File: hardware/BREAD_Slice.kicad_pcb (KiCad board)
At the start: 2 copper layers, 70 x 100 mm, 15 parts, among them J1 Conn_01x10_Female

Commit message: completed schematic and board
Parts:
- added C10: 10u X7R, Capacitor_SMD:C_1206_3216Metric_Pad1.33x1.80mm_HandSolder, F.Cu at (90.9, 107.4)
- added C11: 0.1u X7R, Capacitor_SMD:C_1206_3216Metric_Pad1.33x1.80mm_HandSolder, F.Cu at (94.8, 109.4)
- added C12: 1u X7R, Capacitor_SMD:C_1206_3216Metric_Pad1.33x1.80mm_HandSolder, F.Cu at (97.5, 109.4)
- added C13: 10u X5R, Capacitor_SMD:C_1206_3216Metric_Pad1.33x1.80mm_HandSolder, F.Cu at (86.2, 106.4)
- added C14: 10u, Capacitor_SMD:C_0805_2012Metric_Pad1.18x1.45mm_HandSolder, F.Cu at (67.8, 118.6)
- added C15: 10n, Capacitor_SMD:C_0805_2012Metric_Pad1.18x1.45mm_HandSolder, F.Cu at (67.8, 122.8)
- added C16: 10n, Capacitor_SMD:C_0805_2012Metric_Pad1.18x1.45mm_HandSolder, F.Cu at (82.3, 122.9)
- added C17: 10u, Capacitor_SMD:C_0805_2012Metric_Pad1.18x1.45mm_HandSolder, F.Cu at (79.8, 127.3)
- added C18: 0.01u, Capacitor_SMD:C_0603_1608Metric_Pad1.08x0.95mm_HandSolder, F.Cu at (139.0, 132.9)
- added C19: 0.1u, Capacitor_SMD:C_0603_1608Metric_Pad1.08x0.95mm_HandSolder, F.Cu at (105.1, 104.6)
- added C20: 0.1u, Capacitor_SMD:C_0603_1608Metric_Pad1.08x0.95mm_HandSolder, F.Cu at (105.1, 101.3)
- added C21: 0.01u, Capacitor_SMD:C_0603_1608Metric_Pad1.08x0.95mm_HandSolder, F.Cu at (139.1, 108.9)
- added C22: 0.1u, Capacitor_SMD:C_0603_1608Metric_Pad1.08x0.95mm_HandSolder, F.Cu at (105.0, 98.1)
- added C23: 0.1u, Capacitor_SMD:C_0603_1608Metric_Pad1.08x0.95mm_HandSolder, F.Cu at (105.1, 96.2)
- added C24: 0.01u, Capacitor_SMD:C_0603_1608Metric_Pad1.08x0.95mm_HandSolder, F.Cu at (139.2, 84.5)
- added C25: 0.1u, Capacitor_SMD:C_0603_1608Metric_Pad1.08x0.95mm_HandSolder, F.Cu at (104.6, 91.3)
- added C26: 0.1u, Capacitor_SMD:C_0603_1608Metric_Pad1.08x0.95mm_HandSolder, F.Cu at (102.7, 91.3)
- added C27: 0.01u, Capacitor_SMD:C_0603_1608Metric_Pad1.08x0.95mm_HandSolder, F.Cu at (117.1, 54.6)
- added C28: 0.1u, Capacitor_SMD:C_0603_1608Metric_Pad1.08x0.95mm_HandSolder, F.Cu at (99.5, 91.3)
- added C29: 0.1u, Capacitor_SMD:C_0603_1608Metric_Pad1.08x0.95mm_HandSolder, F.Cu at (94.8, 91.3)
- added C30: 0.01u, Capacitor_SMD:C_0603_1608Metric_Pad1.08x0.95mm_HandSolder, F.Cu at (89.0, 54.4)
- added C31: 0.1u, Capacitor_SMD:C_0603_1608Metric_Pad1.08x0.95mm_HandSolder, F.Cu at (93.0, 91.3)
- added C32: 0.1u, Capacitor_SMD:C_0603_1608Metric_Pad1.08x0.95mm_HandSolder, F.Cu at (89.9, 91.3)
- added C5: 0.01u, Capacitor_SMD:C_0603_1608Metric_Pad1.08x0.95mm_HandSolder, F.Cu at (139.1, 157.3)
- added C6: 0.1u, Capacitor_SMD:C_0603_1608Metric_Pad1.08x0.95mm_HandSolder, F.Cu at (102.2, 108.8)
- added C7: 0.1u, Capacitor_SMD:C_0603_1608Metric_Pad1.08x0.95mm_HandSolder, F.Cu at (104.1, 108.8)
- added C8: 0.1u X7R, Capacitor_SMD:C_0603_1608Metric_Pad1.08x0.95mm_HandSolder, F.Cu at (87.0, 104.3)
- added C9: 10u X7R, Capacitor_SMD:C_1206_3216Metric_Pad1.33x1.80mm_HandSolder, F.Cu at (86.2, 102.2)
- added D10: DF2S6.8MFS_L3M, Diode_SMD:D_SOD-923, B.Cu at (142.1, 114.4)
- added D11: DF2S6.8MFS_L3M, Diode_SMD:D_SOD-923, B.Cu at (135.4, 114.4)
- added D12: DF2S6.8MFS_L3M, Diode_SMD:D_SOD-923, B.Cu at (142.2, 101.9)
- added D13: DF2S6.8MFS_L3M, Diode_SMD:D_SOD-923, B.Cu at (135.2, 101.9)
- added D14: DF2S6.8MFS_L3M, Diode_SMD:D_SOD-923, B.Cu at (142.1, 90.0)
- added D15: DF2S6.8MFS_L3M, Diode_SMD:D_SOD-923, B.Cu at (135.3, 90.0)
- added D16: DF2S6.8MFS_L3M, Diode_SMD:D_SOD-923, B.Cu at (142.1, 77.6)
- added D17: DF2S6.8MFS_L3M, Diode_SMD:D_SOD-923, B.Cu at (135.2, 77.6)
- added D18: DF2S6.8MFS_L3M, Diode_SMD:D_SOD-923, B.Cu at (122.6, 51.7)
- added D19: DF2S6.8MFS_L3M, Diode_SMD:D_SOD-923, B.Cu at (122.6, 58.4)
- added D2: DF2S6.8MFS_L3M, Diode_SMD:D_SOD-923, B.Cu at (142.0, 162.8)
- added D20: DF2S6.8MFS_L3M, Diode_SMD:D_SOD-923, B.Cu at (110.2, 51.6)
- added D21: DF2S6.8MFS_L3M, Diode_SMD:D_SOD-923, B.Cu at (110.2, 58.6)
- added D22: DF2S6.8MFS_L3M, Diode_SMD:D_SOD-923, B.Cu at (94.5, 51.6)
- added D23: DF2S6.8MFS_L3M, Diode_SMD:D_SOD-923, B.Cu at (94.5, 58.3)
- added D24: DF2S6.8MFS_L3M, Diode_SMD:D_SOD-923, B.Cu at (82.0, 51.5)
- added D25: DF2S6.8MFS_L3M, Diode_SMD:D_SOD-923, B.Cu at (82.0, 58.5)
- added D3: DF2S6.8MFS_L3M, Diode_SMD:D_SOD-923, B.Cu at (135.3, 162.7)
- added D4: DF2S6.8MFS_L3M, Diode_SMD:D_SOD-923, B.Cu at (142.1, 150.3)
- added D5: DF2S6.8MFS_L3M, Diode_SMD:D_SOD-923, B.Cu at (135.1, 150.3)
- added D6: DF2S6.8MFS_L3M, Diode_SMD:D_SOD-923, B.Cu at (142.0, 138.4)
- added D7: DF2S6.8MFS_L3M, Diode_SMD:D_SOD-923, B.Cu at (135.3, 138.4)
- added D8: DF2S6.8MFS_L3M, Diode_SMD:D_SOD-923, B.Cu at (142.1, 126.0)
- added D9: DF2S6.8MFS_L3M, Diode_SMD:D_SOD-923, B.Cu at (135.1, 126.0)
- added J10: PCC-SMP-V-K, kml-custom:OMEGA_PCC-SMP-V-K, F.Cu at (132.3, 126.0)
- added J11: PCC-SMP-V-K, kml-custom:OMEGA_PCC-SMP-V-K, F.Cu at (132.4, 101.9)
- added J12: PCC-SMP-V-K, kml-custom:OMEGA_PCC-SMP-V-K, F.Cu at (132.4, 77.6)
- added J13: PCC-SMP-V-K, kml-custom:OMEGA_PCC-SMP-V-K, F.Cu at (110.1, 61.4)
- added J14: PCC-SMP-V-K, kml-custom:OMEGA_PCC-SMP-V-K, F.Cu at (82.0, 61.3)
- added J2: Conn_01x03_Pin, Connector_PinHeader_2.54mm:PinHeader_1x03_P2.54mm_Vertical, F.Cu at (81.4, 89.7)
- added J3: PCC-SMP-V-K, kml-custom:OMEGA_PCC-SMP-V-K, F.Cu at (132.3, 162.7)
- added J4: PCC-SMP-V-K, kml-custom:OMEGA_PCC-SMP-V-K, F.Cu at (132.3, 138.4)
- added J5: PCC-SMP-V-K, kml-custom:OMEGA_PCC-SMP-V-K, F.Cu at (132.4, 114.4)
- added J6: PCC-SMP-V-K, kml-custom:OMEGA_PCC-SMP-V-K, F.Cu at (132.4, 90.0)
- added J7: PCC-SMP-V-K, kml-custom:OMEGA_PCC-SMP-V-K, F.Cu at (122.6, 61.4)
- added J8: PCC-SMP-V-K, kml-custom:OMEGA_PCC-SMP-V-K, F.Cu at (94.5, 61.3)
- added J9: PCC-SMP-V-K, kml-custom:OMEGA_PCC-SMP-V-K, F.Cu at (132.3, 150.3)
- added NT1: NetTie_2, NetTie:NetTie-2_SMD_Pad2.0mm, B.Cu at (63.7, 156.4)
- added NT2: NetTie_2, NetTie:NetTie-2_SMD_Pad2.0mm, F.Cu at (73.4, 125.4)
- added Q1: 2N3904, Package_TO_SOT_THT:TO-92_Inline, F.Cu at (135.4, 156.9)
- added Q2: 2N3904, Package_TO_SOT_THT:TO-92_Inline, F.Cu at (135.4, 132.5)
- added Q3: 2N3904, Package_TO_SOT_THT:TO-92_Inline, F.Cu at (135.5, 108.5)
- added Q4: 2N3904, Package_TO_SOT_THT:TO-92_Inline, F.Cu at (135.5, 84.2)
- added Q5: 2N3904, Package_TO_SOT_THT:TO-92_Inline, F.Cu at (116.7, 58.3)
- added Q6: 2N3904, Package_TO_SOT_THT:TO-92_Inline, F.Cu at (88.6, 58.2)
- added R1: 1k, Resistor_SMD:R_0603_1608Metric_Pad0.98x0.95mm_HandSolder, F.Cu at (85.0, 93.1)
- added R10: 1k, Resistor_SMD:R_0603_1608Metric_Pad0.98x0.95mm_HandSolder, F.Cu at (117.5, 136.7)
- added R11: 1k, Resistor_SMD:R_0603_1608Metric_Pad0.98x0.95mm_HandSolder, F.Cu at (105.1, 102.8)
- added R12: 1k, Resistor_SMD:R_0603_1608Metric_Pad0.98x0.95mm_HandSolder, F.Cu at (127.0, 126.0)
- added R13: 1k, Resistor_SMD:R_0603_1608Metric_Pad0.98x0.95mm_HandSolder, F.Cu at (105.0, 99.7)
- added R14: 1k, Resistor_SMD:R_0603_1608Metric_Pad0.98x0.95mm_HandSolder, F.Cu at (117.4, 112.6)
- added R15: 1k, Resistor_SMD:R_0603_1608Metric_Pad0.98x0.95mm_HandSolder, F.Cu at (105.1, 94.7)
- added R16: 1k, Resistor_SMD:R_0603_1608Metric_Pad0.98x0.95mm_HandSolder, F.Cu at (127.0, 101.9)
- added R17: 1k, Resistor_SMD:R_0603_1608Metric_Pad0.98x0.95mm_HandSolder, F.Cu at (106.1, 91.3)
- added R18: 1k, Resistor_SMD:R_0603_1608Metric_Pad0.98x0.95mm_HandSolder, F.Cu at (117.6, 88.3)
- added R19: 1k, Resistor_SMD:R_0603_1608Metric_Pad0.98x0.95mm_HandSolder, F.Cu at (101.1, 91.3)
- added R2: 1k, Resistor_SMD:R_0603_1608Metric_Pad0.98x0.95mm_HandSolder, F.Cu at (85.0, 95.8)
- added R20: 1k, Resistor_SMD:R_0603_1608Metric_Pad0.98x0.95mm_HandSolder, F.Cu at (127.0, 77.6)
- added R21: 1k, Resistor_SMD:R_0603_1608Metric_Pad0.98x0.95mm_HandSolder, F.Cu at (98.0, 91.3)
- added R22: 1k, Resistor_SMD:R_0603_1608Metric_Pad0.98x0.95mm_HandSolder, F.Cu at (120.9, 76.3)
- added R23: 1k, Resistor_SMD:R_0603_1608Metric_Pad0.98x0.95mm_HandSolder, F.Cu at (96.4, 91.3)
- added R24: 1k, Resistor_SMD:R_0603_1608Metric_Pad0.98x0.95mm_HandSolder, F.Cu at (110.2, 66.6)
- added R25: 1k, Resistor_SMD:R_0603_1608Metric_Pad0.98x0.95mm_HandSolder, F.Cu at (91.4, 91.3)
- added R26: 1k, Resistor_SMD:R_0603_1608Metric_Pad0.98x0.95mm_HandSolder, F.Cu at (92.7, 76.2)
- added R27: 1k, Resistor_SMD:R_0603_1608Metric_Pad0.98x0.95mm_HandSolder, F.Cu at (88.3, 91.3)
- added R28: 1k, Resistor_SMD:R_0603_1608Metric_Pad0.98x0.95mm_HandSolder, F.Cu at (82.0, 66.7)
- added R3: 1k, Resistor_SMD:R_0603_1608Metric_Pad0.98x0.95mm_HandSolder, F.Cu at (100.6, 108.8)
- added R4: 1k, Resistor_SMD:R_0603_1608Metric_Pad0.98x0.95mm_HandSolder, F.Cu at (117.3, 161.0)
- added R5: 1k, Resistor_SMD:R_0603_1608Metric_Pad0.98x0.95mm_HandSolder, F.Cu at (105.7, 108.8)
- added R6: 1k, Resistor_SMD:R_0603_1608Metric_Pad0.98x0.95mm_HandSolder, F.Cu at (126.9, 150.3)
- added R7: 99, Resistor_SMD:R_0805_2012Metric_Pad1.20x1.40mm_HandSolder, F.Cu at (79.8, 122.9)
- added R8: 99, Resistor_SMD:R_0805_2012Metric_Pad1.20x1.40mm_HandSolder, F.Cu at (79.8, 118.7)
- added R9: 1k, Resistor_SMD:R_0603_1608Metric_Pad0.98x0.95mm_HandSolder, F.Cu at (105.1, 106.2)
- added SW1: SW_DIP_x03, Button_Switch_SMD:SW_DIP_SPSTx03_Slide_6.7x9.18mm_W6.73mm_P2.54mm_LowProfile_JPin, F.Cu at (124.3, 158.5)
- added SW2: SW_DIP_x03, Button_Switch_SMD:SW_DIP_SPSTx03_Slide_6.7x9.18mm_W6.73mm_P2.54mm_LowProfile_JPin, F.Cu at (124.3, 134.1)
- added SW3: SW_DIP_x03, Button_Switch_SMD:SW_DIP_SPSTx03_Slide_6.7x9.18mm_W6.73mm_P2.54mm_LowProfile_JPin, F.Cu at (124.4, 110.1)
- added SW4: SW_DIP_x03, Button_Switch_SMD:SW_DIP_SPSTx03_Slide_6.7x9.18mm_W6.73mm_P2.54mm_LowProfile_JPin, F.Cu at (124.4, 85.7)
- added SW5: SW_DIP_x03, Button_Switch_SMD:SW_DIP_SPSTx03_Slide_6.7x9.18mm_W6.73mm_P2.54mm_LowProfile_JPin, F.Cu at (118.3, 69.4)
- added SW6: SW_DIP_x03, Button_Switch_SMD:SW_DIP_SPSTx03_Slide_6.7x9.18mm_W6.73mm_P2.54mm_LowProfile_JPin, F.Cu at (90.2, 69.3)
- added U2: LTC2983, Package_QFP:LQFP-48_7x7mm_P0.5mm, F.Cu at (95.5, 100.4)
- added U3: TPS7A4901DGNR, kml-custom:DGN8_1P89X1P57, F.Cu at (74.5, 121.8)
- HS1: footprint KML-Custom:Thermal Pad -> kml-custom:Thermal Pad
- U1: value ~ -> AP63205
- moved A1 77.0 mm to (77.6, 138.6)
- moved C1 77.0 mm to (63.8, 160.7)
- moved C2 77.0 mm to (66.1, 167.5)
- moved D1 77.0 mm to (108.1, 176.9)
- moved J1 77.0 mm to (61.2, 119.6)
- moved L1 77.0 mm to (68.8, 164.0)
- moved U1 77.0 mm to (63.7, 164.0)
- moved C3 77.0 mm to (68.8, 160.7)
- moved HS1 77.0 mm to (66.8, 162.7)
- moved H2 77.0 mm to (62.6, 176.0)
- moved C4 77.0 mm to (68.8, 157.6)
- moved Logo1 76.4 mm to (63.2, 113.1)
- moved H1 65.1 mm to (62.6, 41.1)
- moved H4 53.9 mm to (152.6, 175.9)
- moved H3 35.1 mm to (152.7, 41.1)
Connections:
- net /E_STOP renamed /ESTOP
- A1 pad 10: /D7 -> unconnected-(A1-D7-Pad10)
- A1 pad 11: /D8 -> unconnected-(A1-D8-Pad11)
- A1 pad 12: /D9 -> /RESET
- A1 pad 13: /D10 -> /SS
- A1 pad 14: /D11 -> /MOSI
- A1 pad 15: /D12 -> /MISO
- A1 pad 16: /D13 -> /SCK
- A1 pad 18: /AREF -> unconnected-(A1-AREF-Pad18)
- A1 pad 19: /A0 -> unconnected-(A1-A0-Pad19)
- A1 pad 20: /A1 -> unconnected-(A1-A1-Pad20)
- A1 pad 21: /A2 -> unconnected-(A1-A2-Pad21)
- A1 pad 22: /A3 -> unconnected-(A1-A3-Pad22)
- A1 pad 25: /A6 -> unconnected-(A1-A6-Pad25)
- A1 pad 26: /A7 -> unconnected-(A1-A7-Pad26)
- A1 pad 28: /RESET -> unconnected-(A1-~{RESET}-Pad28)
- A1 pad 9: /D6 -> unconnected-(A1-D6-Pad9)
- J1 pad 1: GND -> GNDPWR
- J1 pad 10: GND -> GNDPWR
- J1 pad 5: GND -> GNDPWR
- J1 pad 7: /INT -> unconnected-(J1-Pin_7-Pad7)
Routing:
- net /CH2: track 0.00 -> 102.6 mm
- net GNDA: track 0.00 -> 96.3 mm, vias 0 -> 647
- net /MISO: track 0.00 -> 92.0 mm, vias 0 -> 1
- net /SCK: track 0.00 -> 91.4 mm, vias 0 -> 1
- net /Dual Selectable SE-DE Thermocouple CJC Input1/TC_1+: track 0.00 -> 91.1 mm
- net /MOSI: track 0.00 -> 89.7 mm, vias 0 -> 1
- net /SS: track 0.00 -> 87.2 mm, vias 0 -> 1
- net /RESET: track 0.00 -> 84.9 mm, vias 0 -> 1
- net /CH5: track 0.00 -> 83.4 mm
- net /CH15: track 0.00 -> 71.5 mm
- net /Dual Selectable SE-DE Thermocouple CJC Input2/TC_1+: track 0.00 -> 69.7 mm
- net /CH18: track 0.00 -> 66.1 mm
- net /CH8: track 0.00 -> 63.5 mm
- net +5V: track 104.2 -> 42.4 mm, vias 1 -> 5
- net /Dual Selectable SE-DE Thermocouple CJC Input5/TC_1+: track 0.00 -> 61.7 mm
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- added copper zone on In2.Cu, net +12V
- added copper zone on In2.Cu, net +5V
- added copper zone on In2.Cu, net +5VA
- added copper zone on In1.Cu, net GND
- added copper zone on B.Cu, net GNDA
- added copper zone on F.Cu, net GNDA
- added copper zone on In1.Cu, net GNDA
- added copper zone on In1.Cu, net GNDPWR
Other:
- board size 70 x 100 mm -> 100.1 x 144.9 mm
- copper layers 2 -> 4
- board text added: "*"
- board text added: "1 0 1 = 2SE 0 1 0 = 1DE"
- board text added: "12V->5V DO.Reg"
- board text added: "12V->5V Sw.Reg"
- board text added: "BREAD Slice Precision Thermocupl. SLC_THMX R3 04-2025"
- board text added: "COLD JUNCTION ISOTHERMAL ZONE"
- board text added: "L1 (Top): - Template digital components (Nano, RGB LED) and I²C signals - use minimal ground pours. L2 (Inner 1): - Solid ground plane - split into an upper {dblquote}gndpwr{dblquote} zone (handling 12V returns) and a lower digital ground zone, connected only at the regulator - these can be resized to accommadate additional planes - i.e. decreasing 12V/GNDPWR planes to connector edge and creating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"
- board text added: "PWRGND - GNDA"
- board text added: "PWRGND - GNDD"
- board text added: "↓Thermocouple 10↓"
- board text added: "↓Thermocouple 11↓"
- board text added: "↓Thermocouple 12↓"
- board text added: "↓Thermocouple 1↓"
- board text added: "↓Thermocouple 2↓"
- board text added: "↓Thermocouple 3↓"
- board text added: "↓Thermocouple 4↓"
- board text added: "↓Thermocouple 5↓"
- board text added: "↓Thermocouple 6↓"
- board text added: "↓Thermocouple 7↓"
- board text added: "↓Thermocouple 8↓"
- board text added: "↓Thermocouple 9↓"
- board text removed: "12V->5V Reg"
- board text removed: "5V I2C Connector"
- board text removed: "BREAD Slice Template SLC_TEMP R0 20YY"

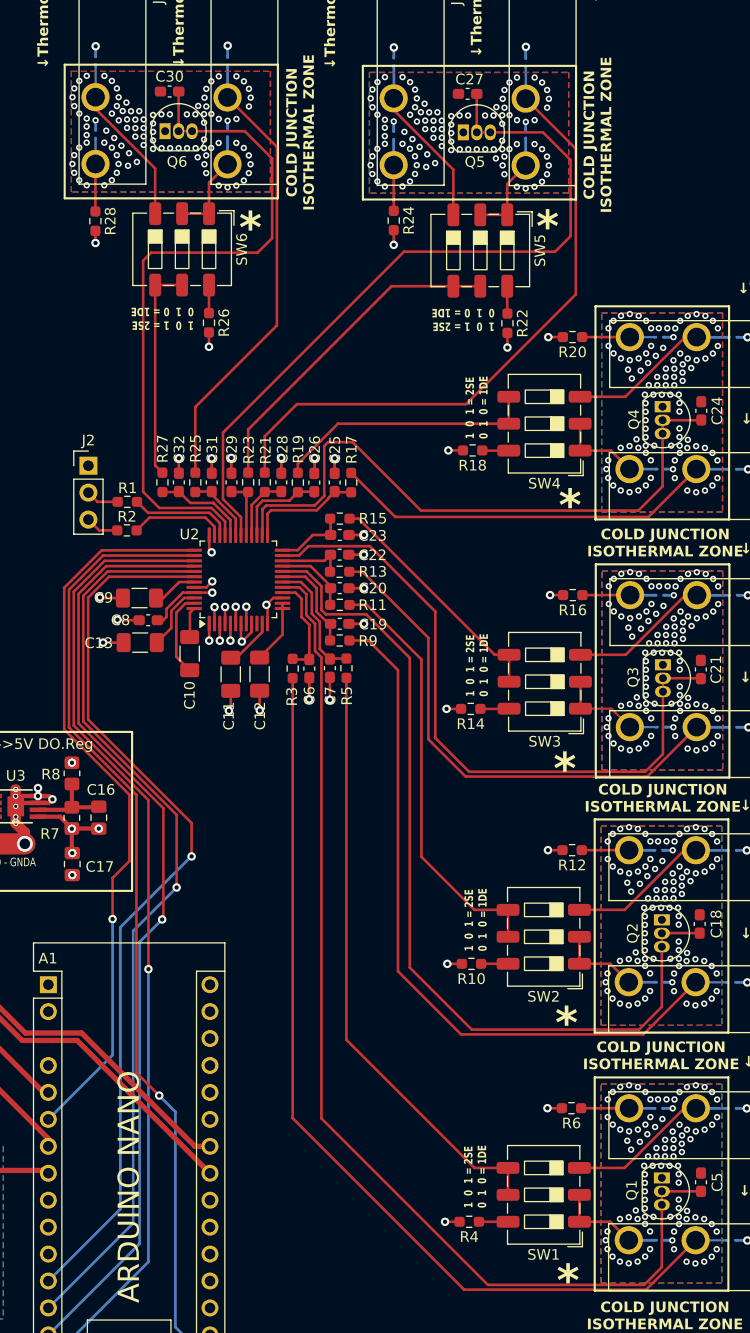
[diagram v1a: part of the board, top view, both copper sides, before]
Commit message: update dip switches to reflect chosen part
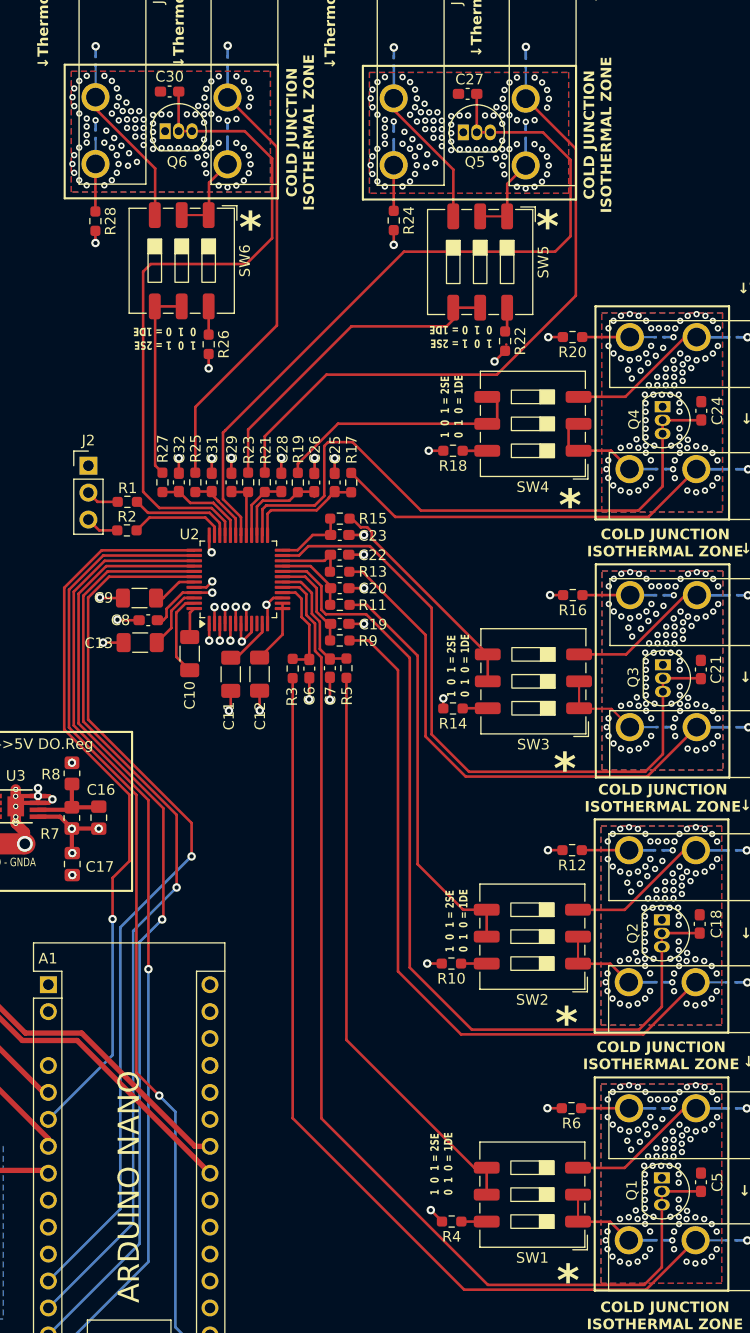
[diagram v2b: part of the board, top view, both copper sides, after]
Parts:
- SW1, SW2, SW3, SW4, SW5, SW6: footprint Button_Switch_SMD:SW_DIP_SPSTx03_Slide_6.7x9.18mm_W6.73mm_P2.54mm_LowProfile_JPin -> Button_Switch_SMD:SW_DIP_SPSTx03_Slide_9.78x9.8mm_W8.61mm_P2.54mm
- moved R26 2.03 mm to (92.7, 78.3)
- moved R10 1.89 mm to (115.6, 136.7)
- moved R18 1.85 mm to (115.7, 88.3)
- moved R22 1.70 mm to (120.7, 78.0)
- moved R14 1.67 mm to (115.7, 112.6)
- moved R4 1.66 mm to (115.6, 161.0)
- moved SW4 1.09 mm to (123.3, 85.8)
- moved SW5 1.09 mm to (118.3, 70.5)
- moved SW6 1.08 mm to (90.2, 70.4)
- moved SW3 1.07 mm to (123.3, 110.0)
- moved SW1 1.07 mm to (123.2, 158.4)
- moved SW2 1.07 mm to (123.2, 134.1)
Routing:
- net /Dual Selectable SE-DE Thermocouple CJC Input4/TC_2+_1-: track 24.8 -> 22.8 mm
- net /Dual Selectable SE-DE Thermocouple CJC Input1/TC_2+_1-: track 56.9 -> 54.9 mm
- net /Dual Selectable SE-DE Thermocouple CJC Input6/TC_2+_1-: track 20.8 -> 18.8 mm
- net /Dual Selectable SE-DE Thermocouple CJC Input3/TC_2+_1-: track 22.9 -> 21.3 mm
- net /Dual Selectable SE-DE Thermocouple CJC Input2/TC_2+_1-: track 40.3 -> 38.9 mm
- net /CH18: track 66.1 -> 65.4 mm
